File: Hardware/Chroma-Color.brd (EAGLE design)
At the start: 160 x 100 mm, 44 parts, among them J1 15-91-1102, J2 87832-6422, J3 1775470-6, U1 EP4CE6E22C8N, U2 ADP3338AKCZ-3.3-RL, U3 ADP3338AKCZ-2.5-RL, U4 NCV565ST12T3G, U5 M25P40-VMN6TPBCT, X1 ASDMB-50.000MHZ-LC-T

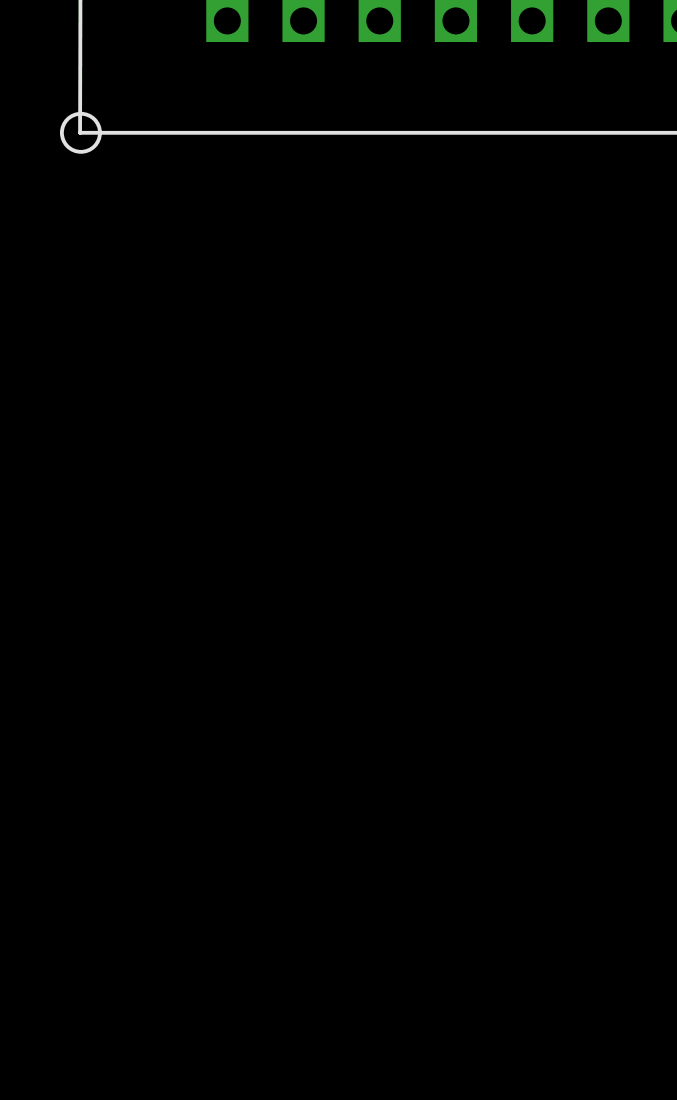
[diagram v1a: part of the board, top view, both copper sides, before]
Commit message: Schematic done, Updated software with latest
Connectors need physical testing before layout happens. DMD connector
needs to be switched to SMT part
D2514-6V0C-AR-WD.
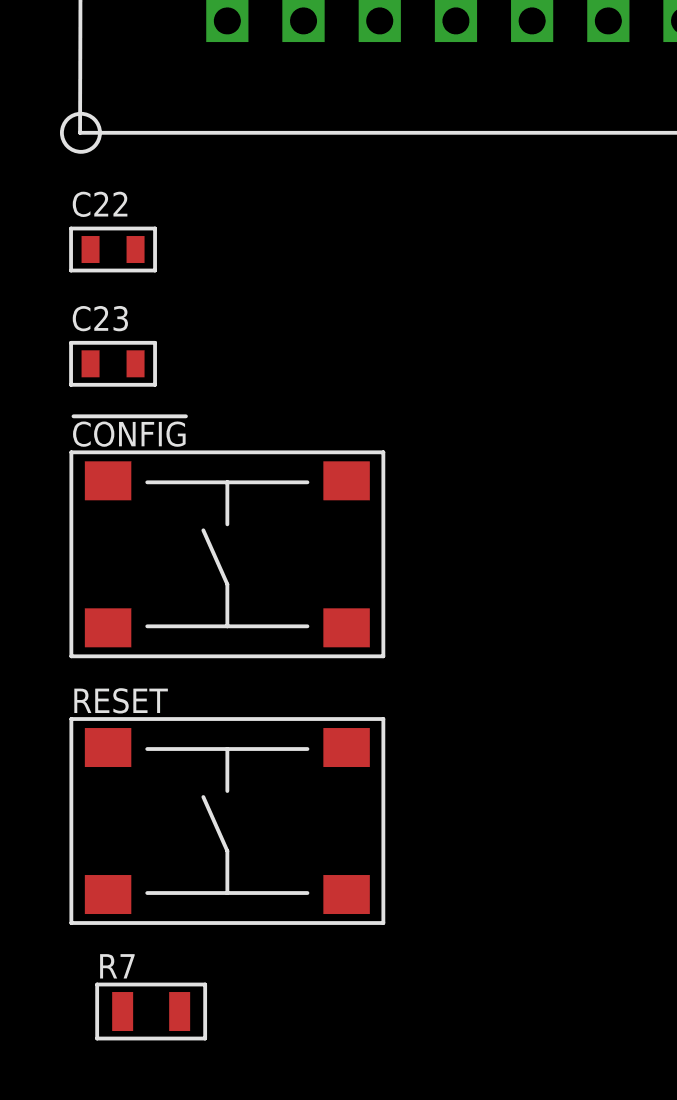
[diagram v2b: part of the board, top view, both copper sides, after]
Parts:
- added !CONFIG, RESET: (no value), MF_Switches:TACT6MM
- added C22, C23: 0.1uF, MF_Passives:C0603
- added R7: 10K, MF_Passives:R0805
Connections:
- net I2V renamed 12V
- removed net N$20: J2.P$27
- new net EVENC-: J2.P$27, U1.120
- new net RESET: R7.P$2, RESET.P$2, U1.125
- net !CONFIG: now also !CONFIG.P$2
- net 2.5V: now also C23.P$1; no longer J1.3, R2.P$2, R3.P$2, R4.P$1, R5.P$1, R6.P$1, U1.96
- net 3.3V: now also C22.P$1, J1.3, R2.P$2, R3.P$2, R4.P$1, R5.P$1, R6.P$1, R7.P$1, U1.96
- net CLK_50: now also U1.25; no longer U1.24
- net CLOCK: now also U1.144
- net DATA: now also U1.143
- net ENABLE: now also U1.135
- net EVEN0+: now also U1.59
- net EVEN0-: now also U1.60
- net EVEN1+: now also U1.70
- net EVEN1-: now also U1.71
- net EVEN2+: now also U1.85
- net EVEN2-: now also U1.84
- net EVENC+: now also U1.121
- net GND: now also !CONFIG.P$4, C22.P$2, C23.P$2, RESET.P$4
- net LATCH: now also U1.142
- net ODD0+: now also U1.38
- net ODD0-: now also U1.39
- net ODD1+: now also U1.49
- net ODD1-: now also U1.50
- net ODD2+: now also U1.52
- net ODD2-: now also U1.53
- net ODDC+: now also U1.54
- net ODDC-: now also U1.55
- net PWM/EN: now also U1.10
- net REG0: now also U1.137
- net REG1: now also U1.138
- net REG2: now also U1.141

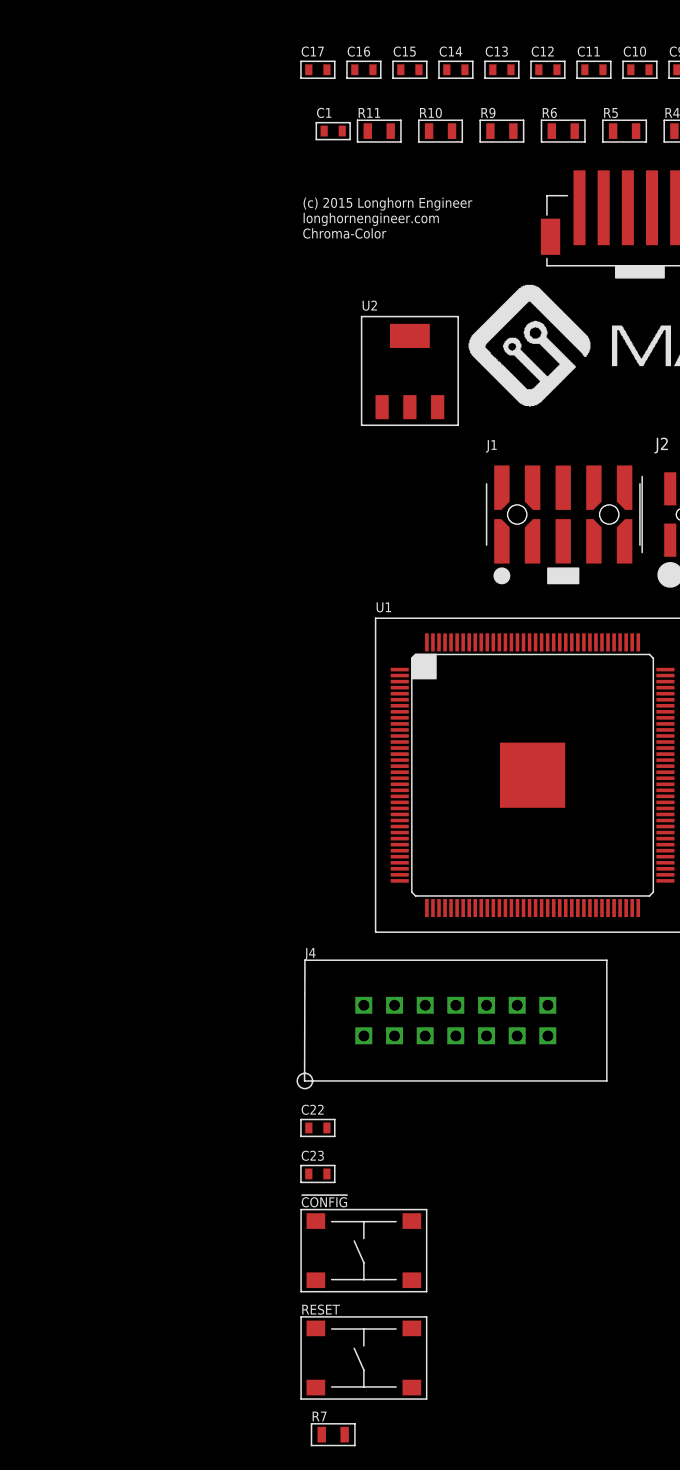
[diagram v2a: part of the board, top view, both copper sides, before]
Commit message: Added last 2x7 SMT connector
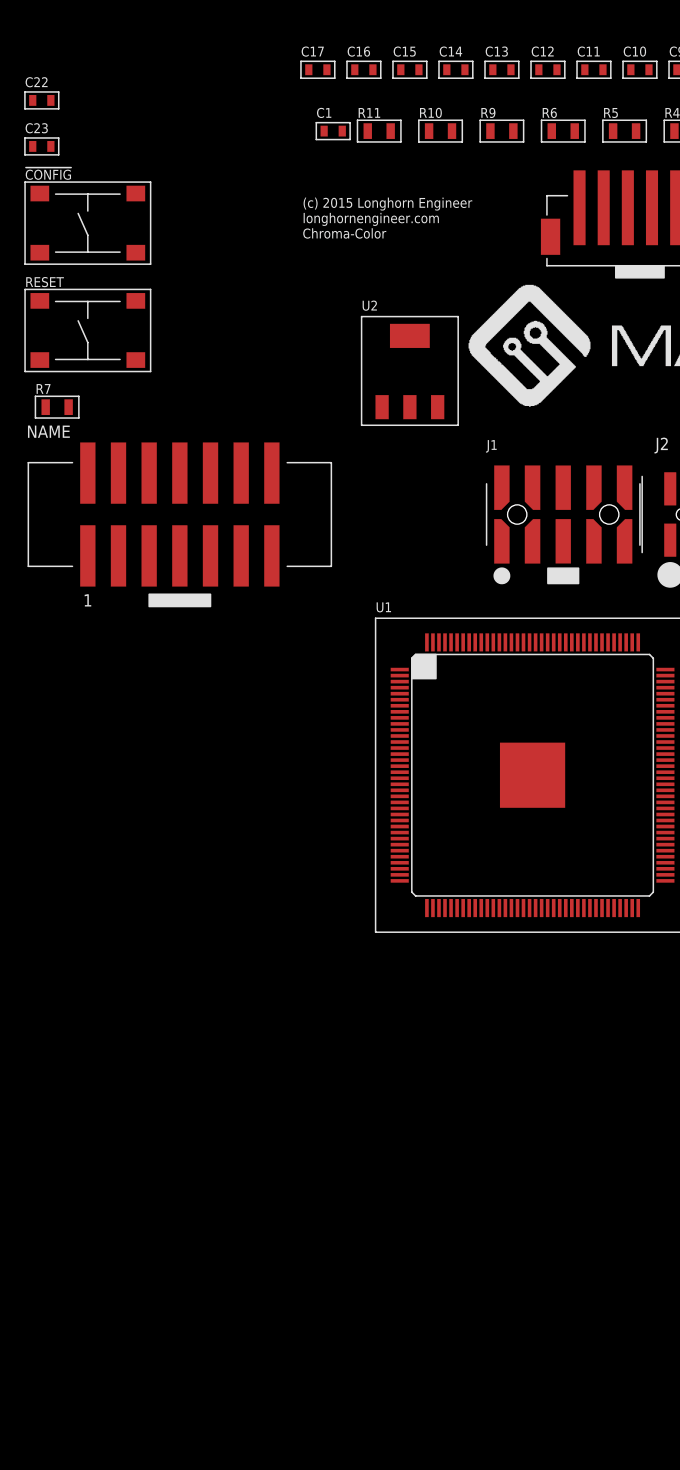
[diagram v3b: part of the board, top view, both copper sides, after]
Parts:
- J4: value (none) -> D2514-6V0C-AR-WD; device PP_Connectors:HEADER_02X07_PTH -> PP_Connectors:D2514-6V0C-AR-WD
- moved !CONFIG 88.1 mm to (-91.4, 59.7)
- moved C23 88.1 mm to (-95.2, 66.0)
- moved R7 88.1 mm to (-94.0, 44.5)
- moved RESET 88.1 mm to (-91.4, 50.8)
- moved C22 88.1 mm to (-95.2, 69.8)
- moved J4 47.7 mm to (-83.8, 35.6)
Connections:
- net DATA: now also J4.3; no longer J4.2
- net ENABLE: now also J4.13; no longer J4.7
- net GND: now also J4.2, J4.4, J4.6; no longer J4.11, J4.13, J4.9
- net LATCH: now also J4.5; no longer J4.3
- net REG0: now also J4.11; no longer J4.6
- net REG1: now also J4.9; no longer J4.5
- net REG2: now also J4.7; no longer J4.4

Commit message: Started Routing.
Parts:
- added J5, J6: (no value), MF_Connectors:PTH_2.54MM_01X34
- moved J4 113.0 mm to (25.4, 64.5)
- moved LOGO1 111.4 mm to (64.8, 40.9)
- moved U1 107.2 mm to (49.5, 39.4)
- moved R7 104.3 mm to (0.76, 0.76), turned to 90 degrees
- moved J2 104.1 mm to (72.4, 12.7)
- moved C23 99.8 mm to (-20.8, -0.51), turned to 90 degrees
- moved C22 99.7 mm to (-24.6, -0.51), turned to 90 degrees
- moved J3 98.9 mm to (40.6, 12.7)
- moved RESET 98.1 mm to (-5.59, 3.30), turned to 90 degrees
- moved U$1 96.4 mm to (10.7, 9.14)
- moved !CONFIG 95.4 mm to (-14.5, 3.30), turned to 90 degrees
- moved U$2 75.5 mm to (10.7, 17.0)
- moved J1 69.4 mm to (17.3, 32.8)
- moved C17 67.4 mm to (-27.2, 22.4), turned to 90 degrees
- moved C1 65.7 mm to (-22.1, 23.6), turned to 90 degrees
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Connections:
- new net PIN_1: J5.P$1, U1.1
- new net PIN_100: J6.P$4, U1.100
- new net PIN_101: J6.P$5, U1.101
- new net PIN_103: J6.P$6, U1.103
- new net PIN_104: J6.P$7, U1.104
- new net PIN_105: J6.P$8, U1.105
- new net PIN_106: J6.P$9, U1.106
- new net PIN_11: J5.P$5, U1.11
- new net PIN_110: J6.P$10, U1.110
- new net PIN_111: J6.P$11, U1.111
- new net PIN_112: J6.P$12, U1.112
- new net PIN_113: J6.P$13, U1.113
- new net PIN_114: J6.P$14, U1.114
- new net PIN_115: J6.P$15, U1.115
- new net PIN_119: J6.P$16, U1.119
- new net PIN_124: J6.P$17, U1.124
- new net PIN_126: J6.P$18, U1.126
- new net PIN_127: J6.P$19, U1.127
- new net PIN_128: J6.P$20, U1.128
- new net PIN_129: J6.P$21, U1.129
- new net PIN_132: J6.P$22, U1.132
- new net PIN_133: J6.P$23, U1.133
- new net PIN_136: J6.P$24, U1.136
- new net PIN_2: J5.P$2, U1.2
- new net PIN_23: J6.P$30, U1.23
- new net PIN_24: J6.P$29, U1.24
- new net PIN_28: J5.P$6, U1.28
- new net PIN_3: J5.P$3, U1.3
- new net PIN_30: J5.P$7, U1.30
- new net PIN_31: J5.P$8, U1.31
- new net PIN_32: J5.P$9, U1.32
- new net PIN_33: J5.P$10, U1.33
- new net PIN_34: J5.P$11, U1.34
- new net PIN_42: J5.P$12, U1.42
- new net PIN_43: J5.P$13, U1.43
- new net PIN_44: J5.P$14, U1.44
- new net PIN_46: J5.P$15, U1.46
- new net PIN_51: J5.P$16, U1.51
- new net PIN_58: J5.P$17, U1.58
- new net PIN_64: J5.P$18, U1.64
- new net PIN_65: J5.P$19, U1.65
- new net PIN_66: J5.P$20, U1.66
- new net PIN_67: J5.P$21, U1.67
- new net PIN_68: J5.P$22, U1.68
- new net PIN_69: J5.P$23, U1.69
- new net PIN_7: J5.P$4, U1.7
- new net PIN_72: J5.P$24, U1.72
- new net PIN_73: J5.P$25, U1.73
- new net PIN_74: J5.P$26, U1.74
- new net PIN_75: J5.P$27, U1.75
- new net PIN_76: J5.P$28, U1.76
- new net PIN_77: J5.P$29, U1.77
- new net PIN_80: J5.P$30, U1.80
- new net PIN_83: J5.P$31, U1.83
- new net PIN_86: J5.P$32, U1.86
- new net PIN_87: J6.P$1, U1.87
- new net PIN_88: J6.P$25, U1.88
- new net PIN_89: J6.P$26, U1.89
- new net PIN_90: J6.P$27, U1.90
- new net PIN_91: J6.P$28, U1.91
- new net PIN_98: J6.P$2, U1.98
- new net PIN_99: J6.P$3, U1.99
- net 3.3V: now also J5.P$34, J6.P$34
- net EVEN1+: now also J2.P$22; no longer J2.P$21
- net EVEN1-: now also J2.P$21; no longer J2.P$22
- net GND: now also J5.P$33, J6.P$33
- net ODD2+: now also J2.P$12; no longer J2.P$11
- net ODD2-: now also J2.P$11; no longer J2.P$12
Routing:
- net EVENC-: track 0.00 -> 77.8 mm
- net EVENC+: track 0.00 -> 74.6 mm
- net EVEN2-: track 0.00 -> 45.6 mm, vias 0 -> 2
- net EVEN0-: track 0.00 -> 39.1 mm
- net ODD0-: track 0.00 -> 38.5 mm
- net EVEN2+: track 0.00 -> 37.8 mm
- net ODDC-: track 0.00 -> 37.8 mm
- net GND: track 0.00 -> 36.5 mm, vias 0 -> 10
- net PWM/EN: track 0.00 -> 36.2 mm, vias 0 -> 2
- net ODD1-: track 0.00 -> 35.1 mm
- net ODD2-: track 0.00 -> 35.0 mm
- net EVEN1-: track 0.00 -> 34.8 mm
- net EVEN0+: track 0.00 -> 34.2 mm
- net ODD0+: track 0.00 -> 33.7 mm
- net ODDC+: track 0.00 -> 32.9 mm
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- added copper zone on layer 15, net 3.3V
- added copper zone on layer 2, net GND
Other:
- board outline removed

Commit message: Layout complete. Silkscreen next.
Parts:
- removed J5, J6: (no value), MF_Connectors:PTH_2.54MM_01X34
- added C24: 10uF, MF_Passives:C0603
- added C25, C26, C27, C28, C29, C30, C31, C32, C33, C34, C35, C36, C37, C38: 0.1uF, MF_Passives:C0603
- added J7: 26-64-4040, PP_Connectors:MOLEX_KK_4_P1
- !CONFIG, RESET: device MF_Switches:TACT6MM -> MF_Switches:TACT4.2MM
- C16: value 10uF -> 0.1uF
- C9: value 0.1uF -> 100uF; device MF_Passives:C0603 -> MF_Passives:CP6.3MM
- moved C8 115.7 mm to (86.4, 34.5), turned to 0 degrees
- moved C14 113.5 mm to (86.4, 32.8), turned to 0 degrees
- moved C7 112.9 mm to (82.3, 32.8), turned to 180 degrees
- moved C9 112.9 mm to (83.1, 28.4)
- moved R1 111.3 mm to (76.5, 16.3), turned to 180 degrees
- moved C12 109.7 mm to (82.3, 34.5), turned to 180 degrees
- moved R2 107.0 mm to (76.5, 21.3), turned to 0 degrees
- moved C11 104.7 mm to (77.0, 34.5), turned to 0 degrees
- moved C15 104.2 mm to (77.0, 32.8), turned to 0 degrees
- moved C19 103.6 mm to (63.2, 32.8), turned to 180 degrees
- moved R3 103.5 mm to (76.5, 26.4), turned to 0 degrees
- moved C2 103.4 mm to (58.2, 21.1), turned to 180 degrees
- moved X1 103.2 mm to (61.0, 20.1), turned to 180 degrees
- moved C21 102.6 mm to (61.0, 22.6), turned to 180 degrees
- moved C20 101.4 mm to (63.2, 34.5), turned to 180 degrees
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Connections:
- net EPCS_!CS renamed !CSO
- net EPCS_ASDI renamed ASDO
- net EPCS_DATA renamed DATA0
- net EP_DCLK renamed DCLK
- net 1.2V: now also C30.P$1, C31.P$1, C32.P$1, C33.P$1, C34.P$1, C35.P$1, C36.P$1, C37.P$1, C38.P$1
- net 12V: now also J7.2
- net 2.5V: now also C10.P$1
- net 3.3V: now also C25.P$1, C26.P$1, C27.P$1, C28.P$1, C29.P$1; no longer J5.P$34, J6.P$34
- net 5V: now also C24.P$1, J7.3; no longer C10.P$1
- net GND: now also C24.P$2, C25.P$2, C26.P$2, C27.P$2, C28.P$2, C29.P$2, C30.P$2, C31.P$2, C32.P$2, C33.P$2, C34.P$2, C35.P$2, C36.P$2, C37.P$2, C38.P$2, J7.4; no longer J5.P$33, J6.P$33
- net PIN_1: no longer J5.P$1
- net PIN_100: no longer J6.P$4
- net PIN_101: no longer J6.P$5
- net PIN_103: no longer J6.P$6
- net PIN_104: no longer J6.P$7
- net PIN_105: no longer J6.P$8
- net PIN_106: no longer J6.P$9
- net PIN_11: no longer J5.P$5
- net PIN_110: no longer J6.P$10
- net PIN_111: no longer J6.P$11
- net PIN_112: no longer J6.P$12
- net PIN_113: no longer J6.P$13
- net PIN_114: no longer J6.P$14
- net PIN_115: no longer J6.P$15
- net PIN_119: no longer J6.P$16
- net PIN_124: no longer J6.P$17
- net PIN_126: no longer J6.P$18
- net PIN_127: no longer J6.P$19
- net PIN_128: no longer J6.P$20
- net PIN_129: no longer J6.P$21
- net PIN_132: no longer J6.P$22
- net PIN_133: no longer J6.P$23
- net PIN_136: no longer J6.P$24
- net PIN_2: no longer J5.P$2
- net PIN_23: no longer J6.P$30
- net PIN_24: no longer J6.P$29
- net PIN_28: no longer J5.P$6
- net PIN_3: no longer J5.P$3
- net PIN_30: no longer J5.P$7
- net PIN_31: no longer J5.P$8
- net PIN_32: no longer J5.P$9
- net PIN_33: no longer J5.P$10
- net PIN_34: no longer J5.P$11
- net PIN_42: no longer J5.P$12
- net PIN_43: no longer J5.P$13
- net PIN_44: no longer J5.P$14
- net PIN_46: no longer J5.P$15
- net PIN_51: no longer J5.P$16
- net PIN_58: no longer J5.P$17
- net PIN_64: no longer J5.P$18
- net PIN_65: no longer J5.P$19
- net PIN_66: no longer J5.P$20
- net PIN_67: no longer J5.P$21
- net PIN_68: no longer J5.P$22
- net PIN_69: no longer J5.P$23
- net PIN_7: no longer J5.P$4
- net PIN_72: no longer J5.P$24
- net PIN_73: no longer J5.P$25
- net PIN_74: no longer J5.P$26
- net PIN_75: no longer J5.P$27
- net PIN_76: no longer J5.P$28
- net PIN_77: no longer J5.P$29
- net PIN_80: no longer J5.P$30
- net PIN_83: no longer J5.P$31
- net PIN_86: no longer J5.P$32
- net PIN_87: no longer J6.P$1
- net PIN_88: no longer J6.P$25
- net PIN_89: no longer J6.P$26
- net PIN_90: no longer J6.P$27
- net PIN_91: no longer J6.P$28
- net PIN_98: no longer J6.P$2
- net PIN_99: no longer J6.P$3
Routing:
- net GND: track 36.5 -> 213.1 mm, vias 10 -> 62
- net 1.2V: track 0.00 -> 139.9 mm, vias 0 -> 24
- net 3.3V: track 18.6 -> 118.6 mm, vias 7 -> 41
- net !CONFIG: track 0.00 -> 92.9 mm, vias 0 -> 2
- net 2.5V: track 0.00 -> 89.8 mm, vias 0 -> 16
- net 5V: track 0.00 -> 68.0 mm
- net RESET: track 0.00 -> 56.7 mm
- net 12V: track 0.00 -> 55.2 mm
- net ENABLE: track 21.4 -> 51.2 mm
- net REG0: track 22.8 -> 52.6 mm
- net REG1: track 24.7 -> 54.2 mm
- net REG2: track 24.9 -> 50.1 mm
- net LATCH: track 26.9 -> 51.1 mm
- net DATA: track 28.7 -> 52.1 mm
- net CLOCK: track 30.7 -> 53.1 mm
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- added copper zone on layer 1, net 1.2V
- added copper zone on layer 16, net 1.2V
- added copper zone on layer 1, net 2.5V
- added copper zone on layer 16, net 2.5V
- added copper zone on layer 1, net 3.3V
- added copper zone on layer 16, net 3.3V
- added copper zone on layer 1, net GND
- added copper zone on layer 1, net LCD_PWR_M1
- added copper zone on layer 1, net LCD_PWR_M2
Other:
- board outline added: 103.9 x 48 mm
